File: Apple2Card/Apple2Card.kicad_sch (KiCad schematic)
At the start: 57 parts, among them J1 ICSP, J2 Conn_01x25, J3 Conn_01x25, J4 Conn_01x10, J5 Conn_01x04, SW1 SW_Push, U1 ATmega328P-P, U2 74HC32, U3 74HC00, U4 74HC373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

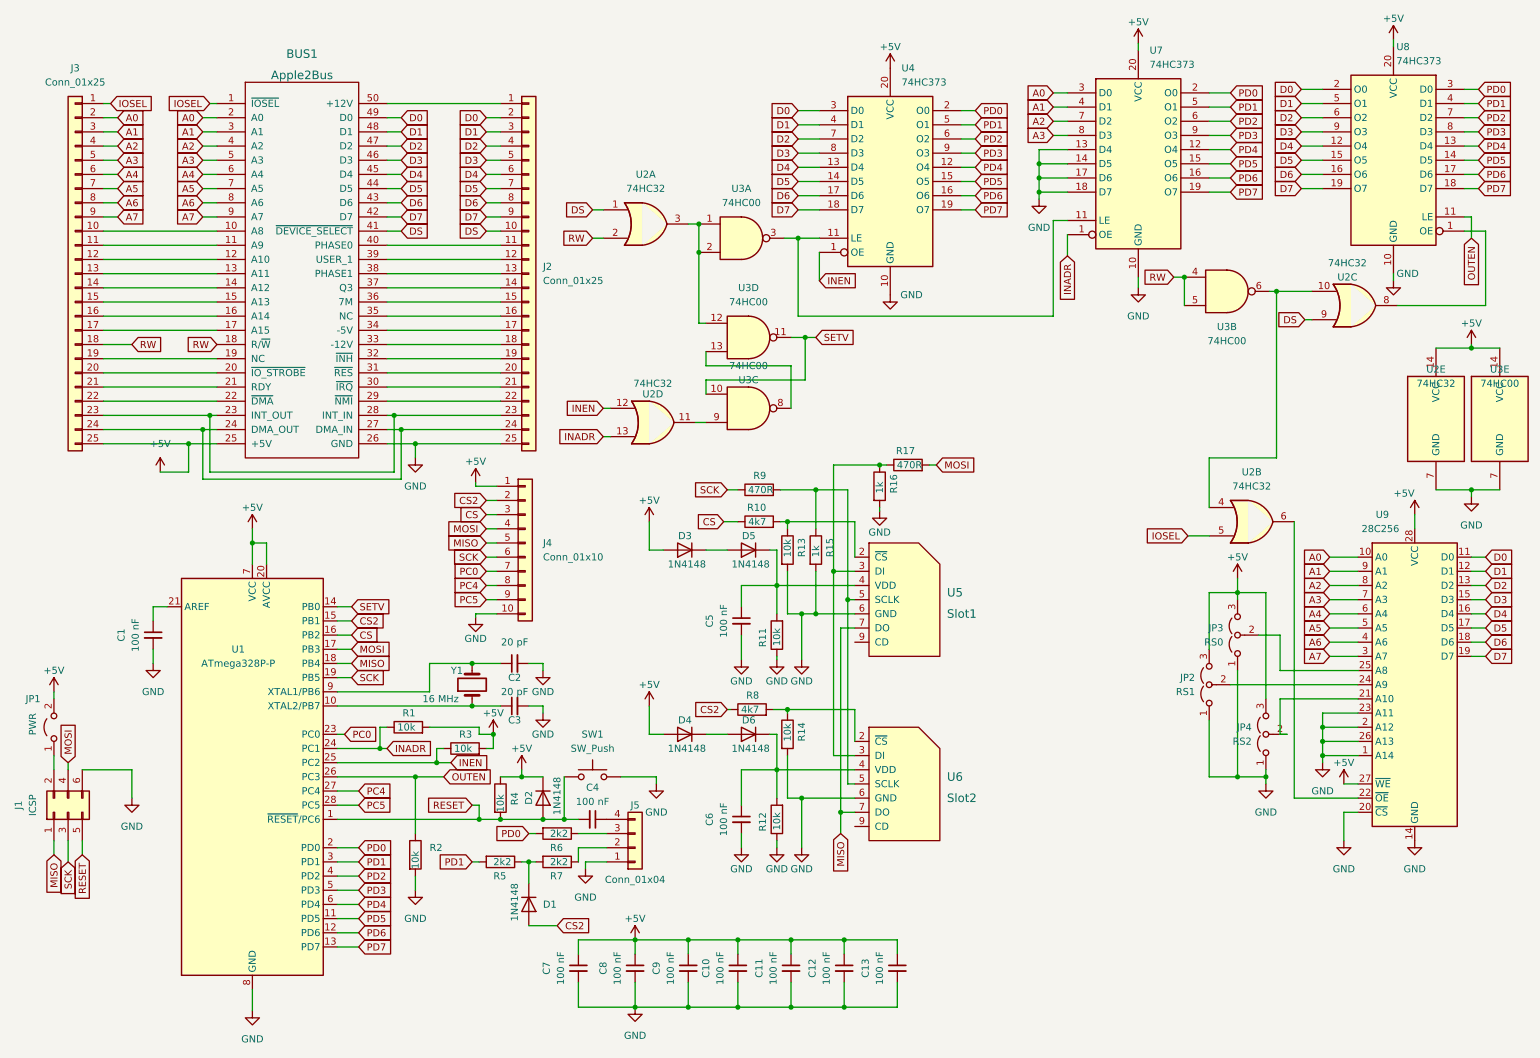
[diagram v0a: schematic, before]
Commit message: Swapped OR with AND
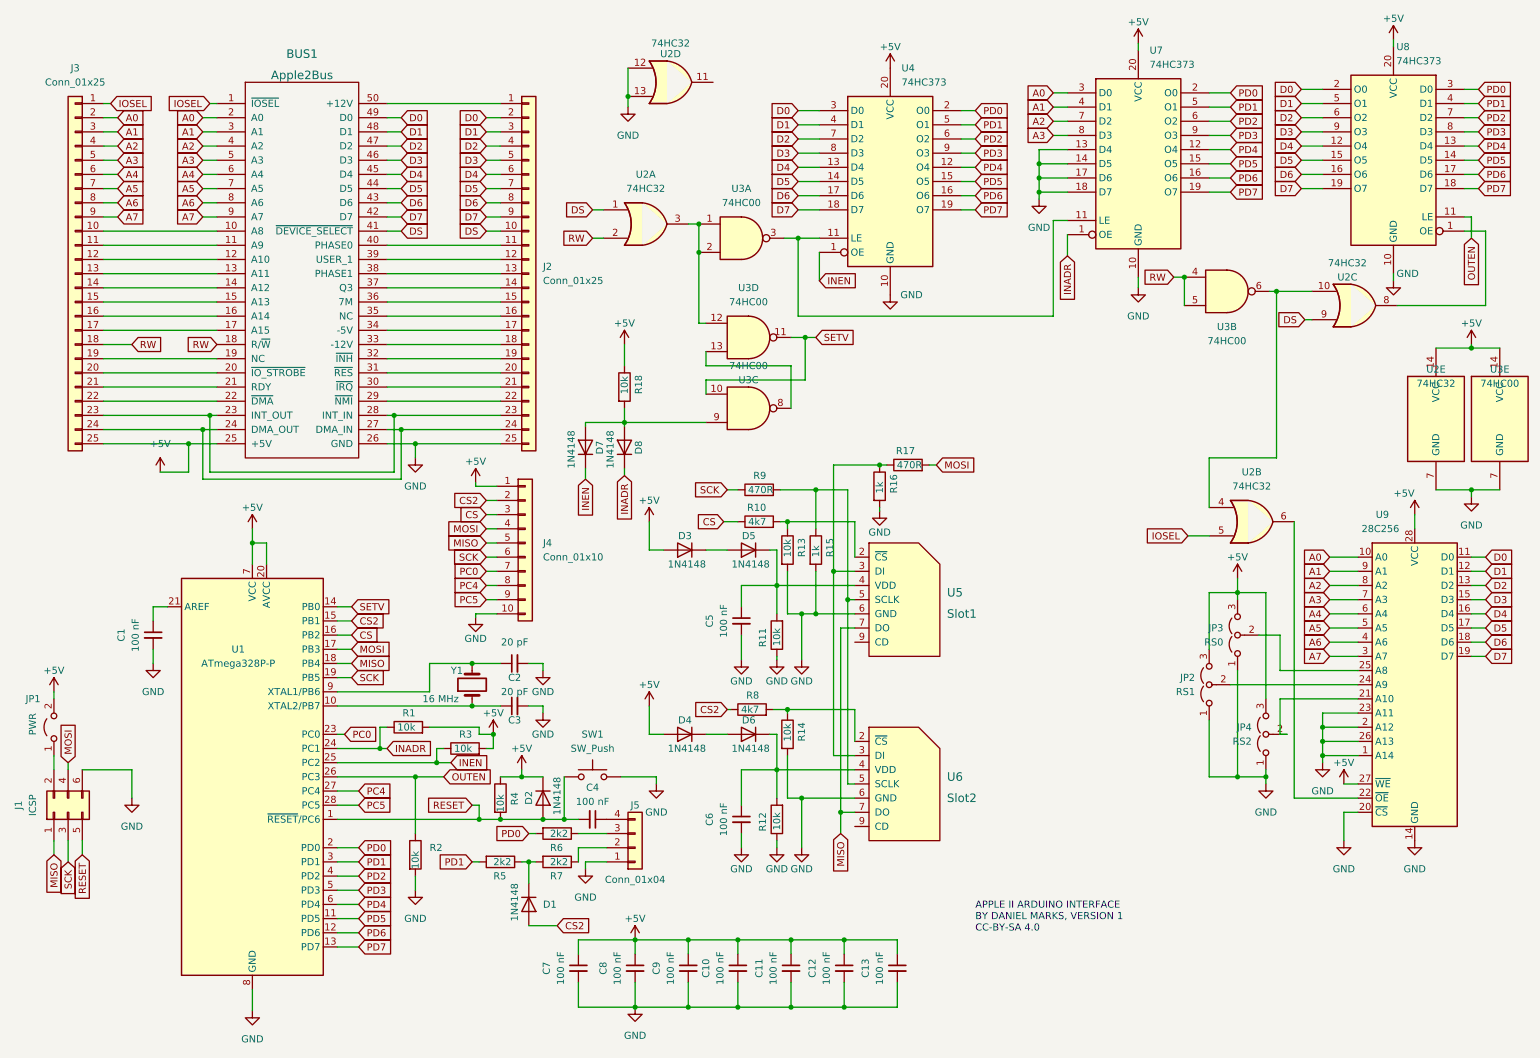
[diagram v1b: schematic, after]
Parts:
- added D7, D8: 1N4148, Diode_THT:D_DO-35_SOD27_P7.62mm_Horizontal, symbol Device:D
- added R18: 10k, Resistor_THT:R_Axial_DIN0207_L6.3mm_D2.5mm_P7.62mm_Horizontal, symbol Device:R
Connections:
- net +5V: now also R18.1
- net GND: now also U2.12, U2.13
- net INADR: now also D8.1 (K); no longer U2.13
- net INEN: now also D7.1 (K); no longer U2.12
- net at U3.9: now also D7.2 (A), D8.2 (A), R18.2; no longer U2.11
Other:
- note added: "APPLE II ARDUINO INTERFACE BY DANIEL MARKS, VERSION 1 CC-BY-SA 4.0"
- moved on the sheet: U2D

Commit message: Add power supply bypass jumpers for power supply variations
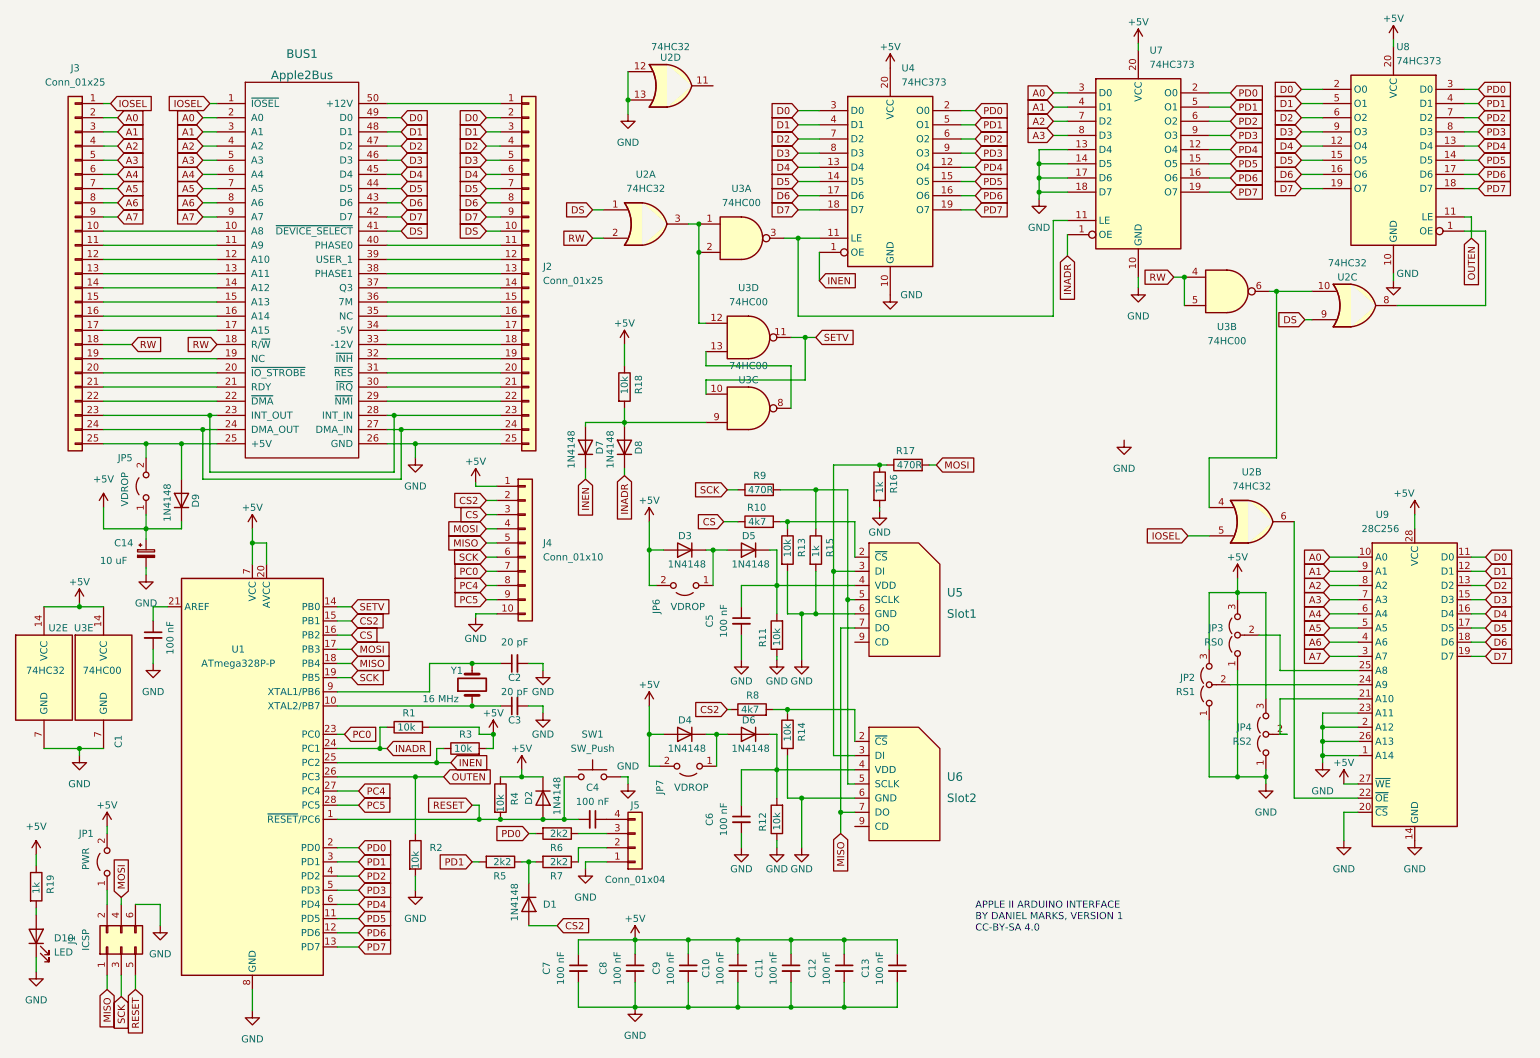
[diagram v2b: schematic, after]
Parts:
- added C14: 10 uF, Capacitor_THT:CP_Radial_D5.0mm_P2.50mm, symbol Device:C_Polarized_Small
- added D10: LED, LED_THT:LED_D3.0mm, symbol Device:LED
- added D9: 1N4148, Diode_THT:D_DO-35_SOD27_P7.62mm_Horizontal, symbol Device:D
- added JP5, JP6, JP7: VDROP, Connector_PinHeader_2.54mm:PinHeader_1x02_P2.54mm_Vertical, symbol Jumper:Jumper_2_Open
- added R19: 1k, Resistor_THT:R_Axial_DIN0207_L6.3mm_D2.5mm_P7.62mm_Horizontal, symbol Device:R
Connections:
- net +5V: now also C14.1, D9.1 (K), JP5.1 (A), JP6.2 (B), JP7.2 (B), R19.1; no longer BUS1.25 (+5V), J3.25 (Pin_25)
- net GND: now also C14.2, D10.1 (K)
- net at D4.1 (K), D6.2 (A): now also JP7.1 (A)
- net at D3.1 (K), D5.2 (A): now also JP6.1 (A)
- new net: BUS1.25 (+5V), D9.2 (A), J3.25 (Pin_25), JP5.2 (B)
- new net: D10.2 (A), R19.2
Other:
- moved on the sheet: J1, JP1, U2D, U2E, U3E

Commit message: Before changing to 8255
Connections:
- net +5V: now also BUS1.25 (+5V), D9.2 (A), J3.25 (Pin_25), JP5.2 (B)
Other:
- moved on the sheet: C10, C13, C14, D9, JP5

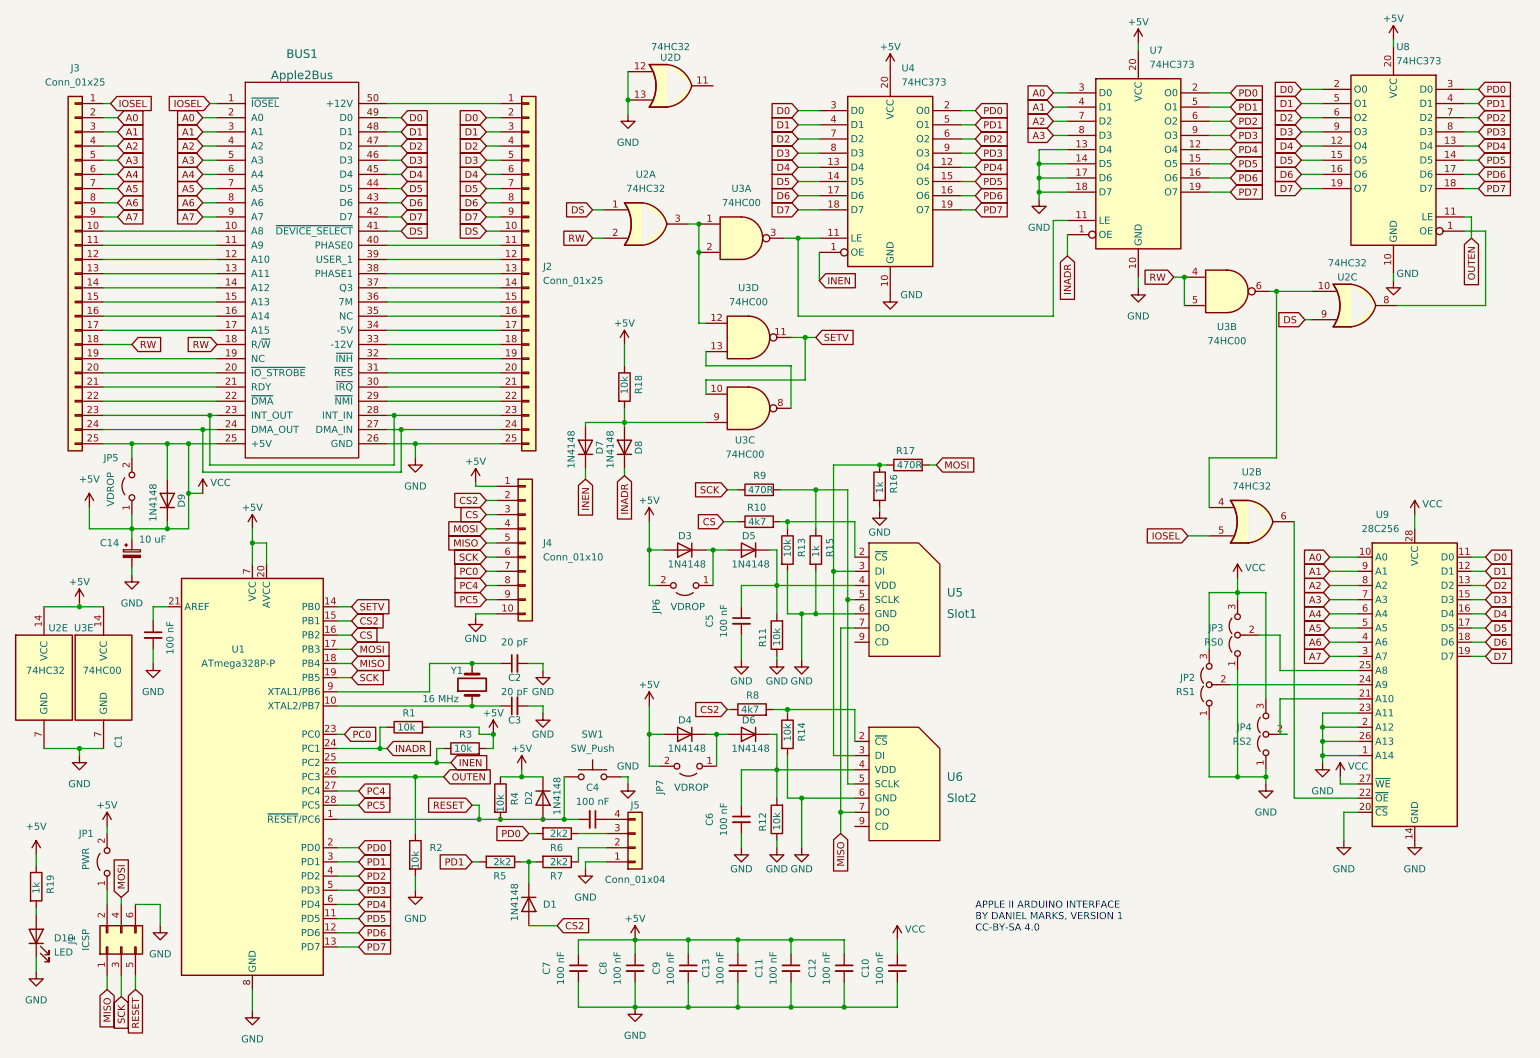
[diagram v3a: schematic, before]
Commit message: Changed to 8255
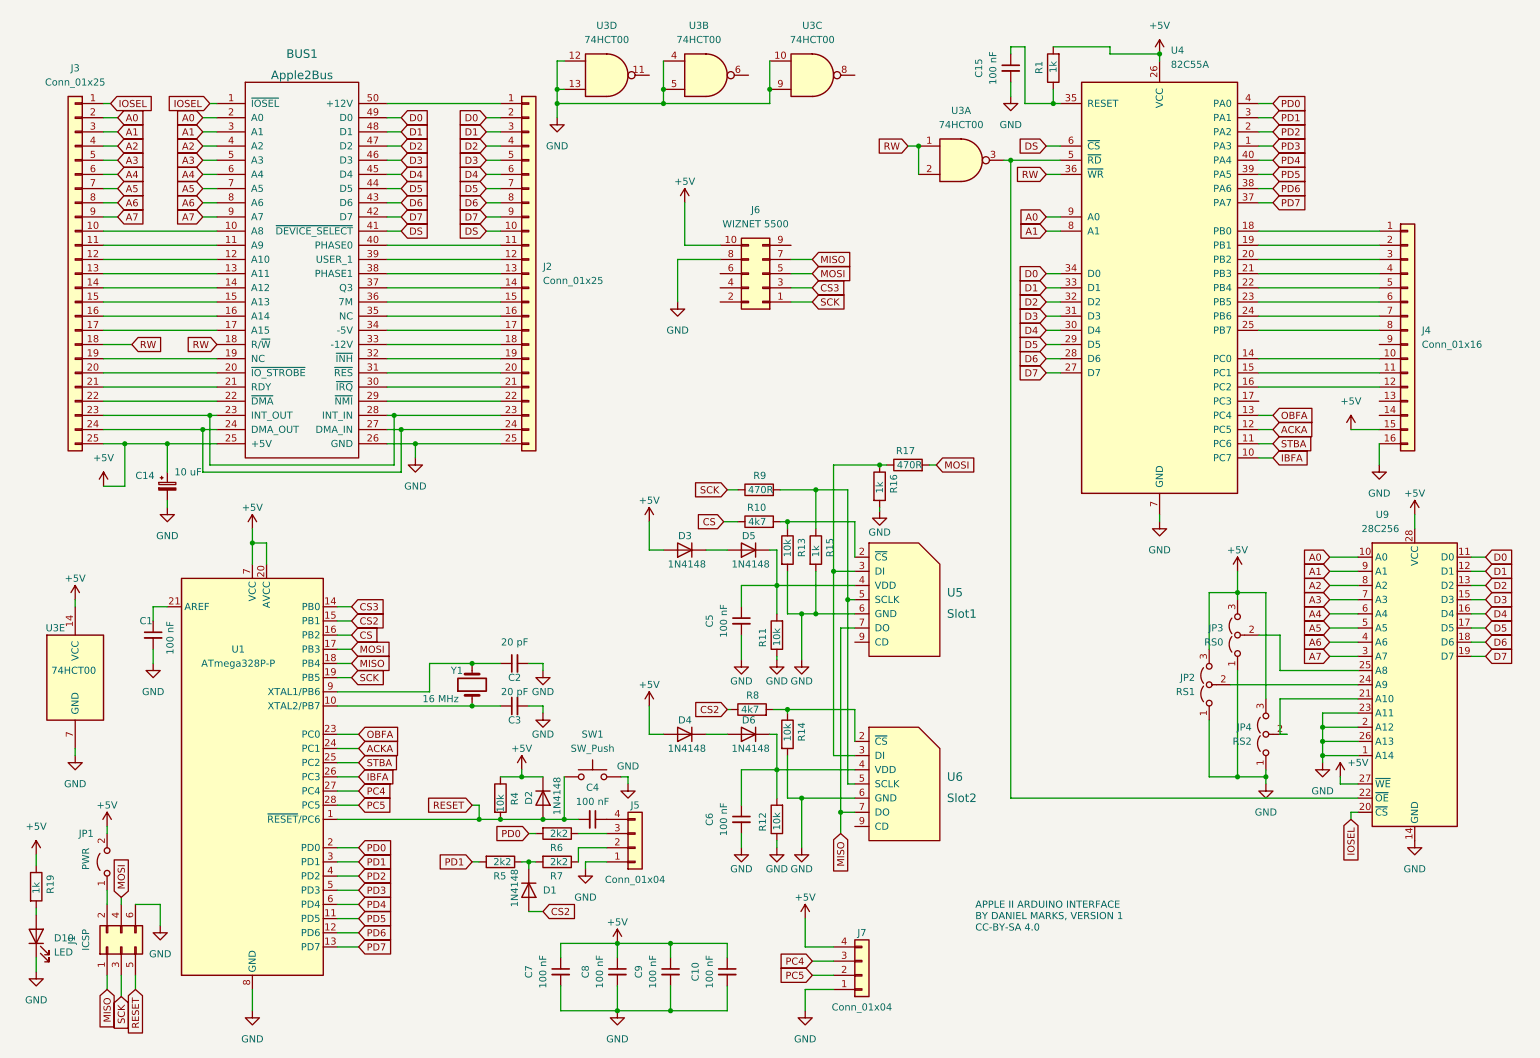
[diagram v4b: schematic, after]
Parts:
- removed C11, C12, C13: 100 nF, Capacitor_THT:C_Disc_D5.0mm_W2.5mm_P5.00mm, symbol Device:C_Small
- removed D7, D8, D9: 1N4148, Diode_THT:D_DO-35_SOD27_P7.62mm_Horizontal, symbol Device:D
- removed J4: Conn_01x10, Connector_PinHeader_2.54mm:PinHeader_1x10_P2.54mm_Vertical, symbol Connector_Generic:Conn_01x10
- removed JP5, JP6, JP7: VDROP, Connector_PinHeader_2.54mm:PinHeader_1x02_P2.54mm_Vertical, symbol Jumper:Jumper_2_Open
- removed R18, R2, R3: 10k, Resistor_THT:R_Axial_DIN0207_L6.3mm_D2.5mm_P7.62mm_Horizontal, symbol Device:R
- removed U2: 74HC32, Package_DIP:DIP-14_W7.62mm_Socket, symbol 74xx:74LS32
- removed U4, U7, U8: 74HC373, Package_DIP:DIP-20_W7.62mm_Socket, symbol 74xx:74HC373
- added C15: 100 nF, Capacitor_THT:C_Disc_D5.0mm_W2.5mm_P5.00mm, symbol Device:C_Small
- added J4: Conn_01x16, Connector_PinHeader_2.54mm:PinHeader_1x16_P2.54mm_Vertical, symbol Connector_Generic:Conn_01x16
- added J6: WIZNET 5500, Connector_PinHeader_2.54mm:PinHeader_2x05_P2.54mm_Vertical, symbol Connector_Generic:Conn_02x05_Odd_Even
- added J7: Conn_01x04, Connector_PinHeader_2.54mm:PinHeader_1x04_P2.54mm_Vertical, symbol Connector_Generic:Conn_01x04
- added U4: 82C55A, Package_DIP:DIP-40_W15.24mm_Socket, symbol Interface:82C55A
- R1: value 10k -> 1k
- U3: value 74HC00 -> 74HCT00
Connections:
- net +5V: now also J4.15 (Pin_15), J6.10 (Pin_10), J7.4 (Pin_4), U4.26 (VCC)
- net A0: now also U4.9 (A0)
- net A1: now also U4.8 (A1)
- net D0: now also U4.34 (D0)
- net D1: now also U4.33 (D1)
- net D2: now also U4.32 (D2)
- net D3: now also U4.31 (D3)
- net D4: now also U4.30 (D4)
- net D5: now also U4.29 (D5)
- net D6: now also U4.28 (D6)
- net D7: now also U4.27 (D7)
- net DS: now also U4.6 (~{CS})
- net GND: now also U3.10, U3.12, U3.13, U3.4, U3.5, U3.9, C15.2, J4.16 (Pin_16), J6.8 (Pin_8), J7.1 (Pin_1), U4.7 (GND); no longer U9.20 (~{CS})
- net IOSEL: now also U9.20 (~{CS})
- net MISO: now also J6.7 (Pin_7)
- net MOSI: now also J6.5 (Pin_5)
- net PC4: now also J7.3 (Pin_3)
- net PC5: now also J7.2 (Pin_2)
- net PD0: now also U4.4 (PA0)
- net PD1: now also U4.3 (PA1)
- net PD2: now also U4.2 (PA2)
- net PD3: now also U4.1 (PA3)
- net PD4: now also U4.40 (PA4)
- net PD5: now also U4.39 (PA5)
- net PD6: now also U4.38 (PA6)
- net PD7: now also U4.37 (PA7)
- net RW: now also U3.1, U3.2, U4.36 (~{WR}); no longer U3.4, U3.5
- net SCK: now also J6.1 (Pin_1)
- net at U3.3: now also U9.22 (~{OE}), U4.5 (~{RD})
- net at U3.8: no longer U3.13
- net INADR: no longer names the net of R1.1
- net INADR: now also C15.1, U4.35 (RESET); no longer U1.24 (PC1)
- net INEN renamed STBA
- net STBA: now also U4.11 (PC6)
- net OUTEN renamed IBFA
- net IBFA: now also U4.10 (PC7)
- net PC0 renamed OBFA
- net OBFA: now also U4.13 (PC4)
- removed net SETV: U1.14 (PB0), U3.10, U3.11
- new net: J4.1 (Pin_1), U4.18 (PB0)
- new net: J4.10 (Pin_10), U4.14 (PC0)
- new net: J4.11 (Pin_11), U4.15 (PC1)
- new net: J4.12 (Pin_12), U4.16 (PC2)
- new net: J4.2 (Pin_2), U4.19 (PB1)
- new net: J4.3 (Pin_3), U4.20 (PB2)
- new net: J4.4 (Pin_4), U4.21 (PB3)
- new net: J4.5 (Pin_5), U4.22 (PB4)
- new net: J4.6 (Pin_6), U4.23 (PB5)
- new net: J4.7 (Pin_7), U4.24 (PB6)
- new net: J4.8 (Pin_8), U4.25 (PB7)
- new net ACKA: U1.24 (PC1), U4.12 (PC5)
- new net CS3: J6.3 (Pin_3), U1.14 (PB0)
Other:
- moved on the sheet: C10, C14, C7, C8, C9, D1, U3A, U3B, U3C, U3D, U3E
